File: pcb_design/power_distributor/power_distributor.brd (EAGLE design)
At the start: 34.3 x 34.3 mm, 12 parts

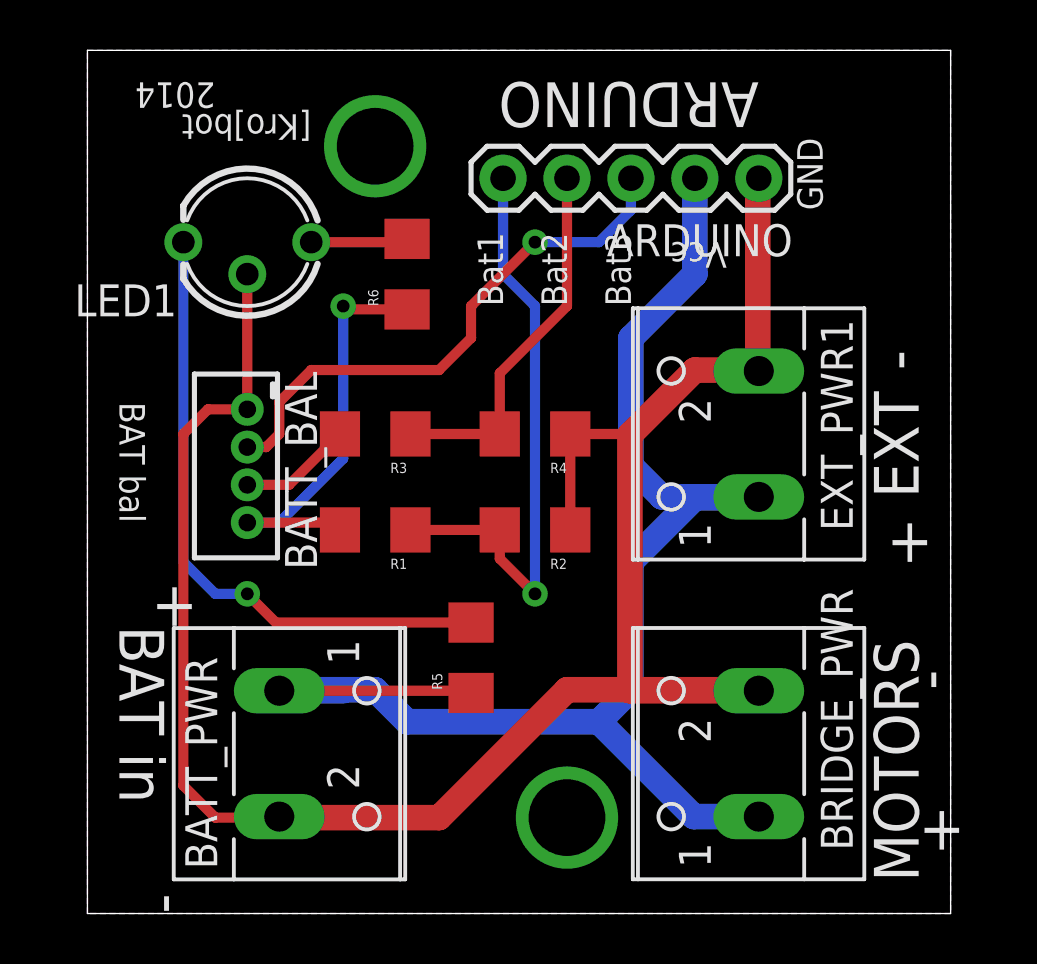
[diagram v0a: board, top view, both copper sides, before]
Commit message: [PCB/power_distributor] Correcting wrong JST footprint
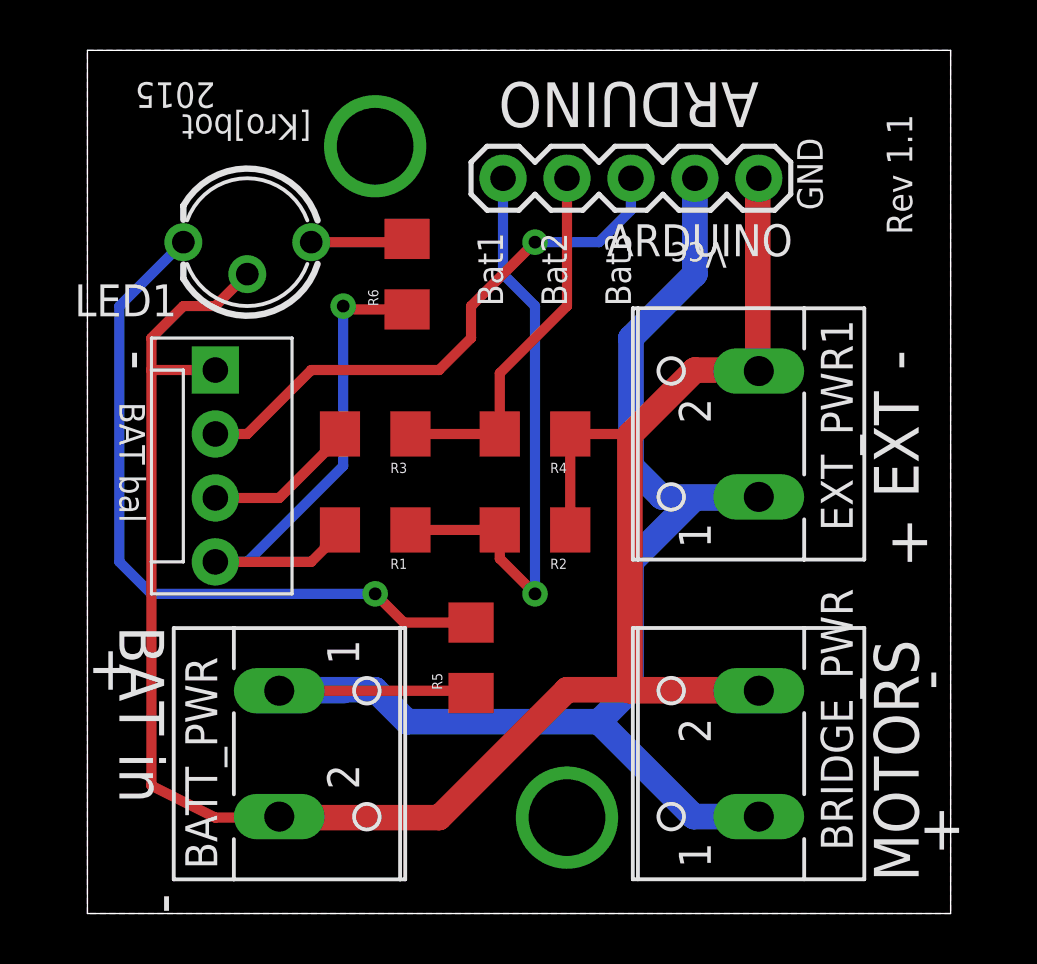
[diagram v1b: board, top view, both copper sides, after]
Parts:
- BATT_BAL: value B4B-ZR -> (none); device con-jst:B4B-ZR -> SparkFun-Connectors:MOLEX-1X4
- moved BATT_BAL 4.02 mm to (5.08, 21.6)
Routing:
- net VCC: track 17.3 -> 21.7 mm
- net GND: track 83.2 -> 87.1 mm
- net N$1: track 25.1 -> 28.7 mm
- net N$2: track 4.52 -> 6.08 mm
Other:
- board text added: "2015"
- board text added: "Rev 1.1"
- board text removed: "2014"
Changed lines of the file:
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@@
 <?xml version="1.0" encoding="utf-8"?>
 <!DOCTYPE eagle SYSTEM "eagle.dtd">
-<eagle version="7.1.0">
+<eagle version="6.5.0">
 <drawing>
 <settings>
@@
 <layers>
 <layer number="1" name="Top" color="4" fill="1" visible="yes" active="yes"/>
+<layer number="2" name="Route2" color="1" fill="3" visible="no" active="no"/>
+<layer number="3" name="Route3" color="4" fill="3" visible="no" active="no"/>
+<layer number="4" name="Route4" color="1" fill="4" visible="no" active="no"/>
+<layer number="5" name="Route5" color="4" fill="4" visible="no" active="no"/>
+<layer number="6" name="Route6" color="1" fill="8" visible="no" active="no"/>
+<layer number="7" name="Route7" color="4" fill="8" visible="no" active="no"/>
+<layer number="8" name="Route8" color="1" fill="2" visible="no" active="no"/>
+<layer number="9" name="Route9" color="4" fill="2" visible="no" active="no"/>
+<layer number="10" name="Route10" color="1" fill="7" visible="no" active="no"/>
+<layer number="11" name="Route11" color="4" fill="7" visible="no" active="no"/>
+<layer number="12" name="Route12" color="1" fill="5" visible="no" active="no"/>
+<layer number="13" name="Route13" color="4" fill="5" visible="no" active="no"/>
+<layer number="14" name="Route14" color="1" fill="6" visible="no" active="no"/>
+<layer number="15" name="Route15" color="4" fill="6" visible="no" active="no"/>
 <layer number="16" name="Bottom" color="1" fill="1" visible="yes" active="yes"/>
 <layer number="17" name="Pads" color="2" fill="1" visible="yes" active="yes"/>
@@
 <text x="19.05" y="24.13" size="1.016" layer="21" font="vector" ratio="15" rot="R90">Bat2</text>
 <text x="8.89" y="31.75" size="1.016" layer="21" font="vector" ratio="15" rot="SR180">[Kro]bot</text>
-<text x="5.08" y="33.02" size="1.016" layer="21" font="vector" ratio="15" rot="SR180">2014</text>
-<text x="2.54" y="11.43" size="1.778" layer="21" font="vector" ratio="15">+</text>
+<text x="5.08" y="33.02" size="1.016" layer="21" font="vector" ratio="15" rot="SR180">2015</text>
+<text x="0" y="8.89" size="1.778" layer="21" font="vector" ratio="15">+</text>
 <text x="33.02" y="2.54" size="1.778" layer="21" font="vector" ratio="15">+</text>
 <text x="31.75" y="13.97" size="1.778" layer="21" font="vector" ratio="15">+</text>
@@
 <dimension x1="0" y1="34.29" x2="0" y2="0" x3="-5.08" y3="17.145" textsize="1.778" textratio="15" layer="150"/>
 <dimension x1="0" y1="0" x2="34.29" y2="0" x3="17.145" y3="-6.35" textsize="1.778" textratio="15" layer="150"/>
+<text x="31.75" y="31.75" size="1.016" layer="21" font="vector" ratio="15" rot="R270">Rev 1.1</text>
+<text x="2.54" y="21.59" size="1.778" layer="21" font="vector" ratio="15" rot="R90">-</text>
 </plain>
 <attributes>
@@
 <pass name="Default">
 <param name="RoutingGrid" value="50mil"/>
-<param name="AutoGrid" value="1"/>
-<param name="Efforts" value="0"/>
-<param name="TopRouterVariant" value="1"/>
 <param name="tpViaShape" value="round"/>
-<param name="PrefDir.1" value="a"/>
+<param name="PrefDir.1" value="|"/>
 <param name="PrefDir.2" value="0"/>
 <param name="PrefDir.3" value="0"/>
@@
 <param name="PrefDir.14" value="0"/>
 <param name="PrefDir.15" value="0"/>
-<param name="PrefDir.16" value="a"/>
+<param name="PrefDir.16" value="-"/>
 <param name="cfVia" value="8"/>
 <param name="cfNonPref" value="5"/>
@@
 <elements>
 <element name="ARDUINO" library="SparkFun-Connectors" package="1X05" value="" x="26.67" y="29.21" rot="R180"/>
-<element name="BATT_BAL" library="con-jst" package="B4B-ZR" value="B4B-ZR" x="6.35" y="17.78" rot="R270">
-<attribute name="OC_NEWARK" value="37K9960" x="6.35" y="17.78" size="1.778" layer="27" rot="R270" display="off"/>
-<attribute name="MPN" value="B4B-ZR(LF)(SN)" x="6.35" y="17.78" size="1.778" layer="27" rot="R270" display="off"/>
-<attribute name="MF" value="FARNELL" x="6.35" y="17.78" size="1.778" layer="27" rot="R270" display="off"/>
-<attribute name="OC_FARNELL" value="1830916" x="6.35" y="17.78" size="1.778" layer="27" rot="R270" display="off"/>
-</element>
 <element name="BATT_PWR" library="con-wago-500" package="W237-102" value="" x="8.89" y="6.35" rot="R270">
 <attribute name="OC_NEWARK" value="70K9898" x="8.89" y="6.35" size="1.778" layer="27" rot="R270" display="off"/>
@@
 <element name="R5" library="SparkFun-Passives" package="1206" value="1000" x="15.24" y="10.16" rot="R90"/>
 <element name="R6" library="SparkFun-Passives" package="1206" value="1000" x="12.7" y="25.4" rot="R90"/>
+<element name="BATT_BAL" library="SparkFun-Connectors" package="MOLEX-1X4" value="" x="5.08" y="21.59" rot="R270"/>
 </elements>
 <signals>
 <signal name="VCC">
-<contactref element="BATT_BAL" pad="4"/>
 <contactref element="R1" pad="2"/>
 <contactref element="R6" pad="1"/>
-<wire x1="6.35" y1="15.53" x2="9.74" y2="15.53" width="0.4064" layer="1"/>
 <wire x1="9.74" y1="15.53" x2="10.03" y2="15.24" width="0.4064" layer="1"/>
 <wire x1="12.7" y1="24" x2="10.29" y2="24" width="0.4064" layer="1"/>
 <wire x1="10.29" y1="24" x2="10.16" y2="24.13" width="0.4064" layer="1"/>
 <via x="10.16" y="24.13" extent="1-16" drill="0.508"/>
-<wire x1="10.16" y1="24.13" x2="10.16" y2="18.07" width="0.4064" layer="16"/>
-<wire x1="10.16" y1="18.07" x2="7.62" y2="15.53" width="0.4064" layer="16"/>
-<wire x1="7.62" y1="15.53" x2="6.35" y2="15.53" width="0.4064" layer="16"/>
+<wire x1="10.16" y1="24.13" x2="10.16" y2="17.78" width="0.4064" layer="16"/>
+<contactref element="BATT_BAL" pad="4"/>
+<wire x1="9.74" y1="15.53" x2="9.74" y2="14.82" width="0.4064" layer="1"/>
+<wire x1="9.74" y1="14.82" x2="8.89" y2="13.97" width="0.4064" layer="1"/>
+<wire x1="8.89" y1="13.97" x2="5.08" y2="13.97" width="0.4064" layer="1"/>
+<wire x1="10.16" y1="17.78" x2="6.35" y2="13.97" width="0.4064" layer="16"/>
+<wire x1="6.35" y1="13.97" x2="5.08" y2="13.97" width="0.4064" layer="16"/>
 </signal>
 <signal name="BATT_1">
@@
 </signal>
 <signal name="N$2">
+<contactref element="R3" pad="2"/>
 <contactref element="BATT_BAL" pad="3"/>
-<contactref element="R3" pad="2"/>
-<wire x1="6.35" y1="17.03" x2="8.01" y2="17.03" width="0.4064" layer="1"/>
-<wire x1="8.01" y1="17.03" x2="10.03" y2="19.05" width="0.4064" layer="1"/>
+<wire x1="10.03" y1="19.05" x2="10.03" y2="18.92" width="0.4064" layer="1"/>
+<wire x1="10.03" y1="18.92" x2="7.62" y2="16.51" width="0.4064" layer="1"/>
+<wire x1="7.62" y1="16.51" x2="5.08" y2="16.51" width="0.4064" layer="1"/>
 </signal>
 <signal name="BATT_2">
@@
 <contactref element="R2" pad="1"/>
 <contactref element="R4" pad="1"/>
-<contactref element="BATT_BAL" pad="1"/>
 <contactref element="BATT_PWR" pad="2"/>
 <contactref element="LED1" pad="CC"/>
@@
 <contactref element="EXT_PWR1" pad="2"/>
 <wire x1="19.18" y1="15.24" x2="19.18" y2="19.05" width="0.4064" layer="1"/>
-<wire x1="6.35" y1="20.03" x2="6.35" y2="25.4" width="0.4064" layer="1"/>
-<wire x1="6.35" y1="20.03" x2="4.79" y2="20.03" width="0.4064" layer="1"/>
-<wire x1="4.79" y1="20.03" x2="3.81" y2="19.05" width="0.4064" layer="1"/>
-<wire x1="3.81" y1="19.05" x2="3.81" y2="5.08" width="0.4064" layer="1"/>
-<wire x1="3.81" y1="5.08" x2="5.08" y2="3.81" width="0.4064" layer="1"/>
+<wire x1="2.54" y1="22.86" x2="2.54" y2="21.59" width="0.4064" layer="1"/>
+<wire x1="2.54" y1="21.59" x2="2.54" y2="5.08" width="0.4064" layer="1"/>
+<wire x1="2.54" y1="5.08" x2="5.08" y2="3.81" width="0.4064" layer="1"/>
 <wire x1="5.08" y1="3.81" x2="7.58" y2="3.81" width="0.4064" layer="1"/>
 <wire x1="7.58" y1="3.81" x2="7.62" y2="3.85" width="0.4064" layer="1"/>
@@
 <vertex x="34.29" y="0"/>
 </polygon>
+<contactref element="BATT_BAL" pad="1"/>
+<wire x1="2.54" y1="22.86" x2="3.81" y2="24.13" width="0.4064" layer="1"/>
+<wire x1="3.81" y1="24.13" x2="5.08" y2="24.13" width="0.4064" layer="1"/>
+<wire x1="5.08" y1="24.13" x2="6.35" y2="25.4" width="0.4064" layer="1"/>
+<wire x1="5.08" y1="21.59" x2="2.54" y2="21.59" width="0.4064" layer="1"/>
 </signal>
 <signal name="BATT_3">
-<contactref element="BATT_BAL" pad="2"/>
 <contactref element="ARDUINO" pad="3"/>
-<wire x1="6.35" y1="18.53" x2="7.1" y2="18.53" width="0.4064" layer="1"/>
-<wire x1="7.1" y1="18.53" x2="7.62" y2="19.05" width="0.4064" layer="1"/>
-<wire x1="7.62" y1="19.05" x2="7.62" y2="20.32" width="0.4064" layer="1"/>
-<wire x1="7.62" y1="20.32" x2="8.89" y2="21.59" width="0.4064" layer="1"/>
 <wire x1="8.89" y1="21.59" x2="13.97" y2="21.59" width="0.4064" layer="1"/>
 <wire x1="13.97" y1="21.59" x2="15.24" y2="22.86" width="0.4064" layer="1"/>
@@
 <wire x1="20.32" y1="26.67" x2="21.59" y2="27.94" width="0.4064" layer="16"/>
 <wire x1="21.59" y1="27.94" x2="21.59" y2="29.21" width="0.4064" layer="16"/>
+<contactref element="BATT_BAL" pad="2"/>
+<wire x1="8.89" y1="21.59" x2="6.35" y2="19.05" width="0.4064" layer="1"/>
+<wire x1="6.35" y1="19.05" x2="5.08" y2="19.05" width="0.4064" layer="1"/>
 </signal>
 <signal name="VDD">
@@
 <contactref element="R5" pad="2"/>
 <contactref element="LED1" pad="AO"/>
-<wire x1="15.24" y1="11.56" x2="7.49" y2="11.56" width="0.4064" layer="1"/>
-<wire x1="7.49" y1="11.56" x2="6.35" y2="12.7" width="0.4064" layer="1"/>
-<via x="6.35" y="12.7" extent="1-16" drill="0.508"/>
-<wire x1="6.35" y1="12.7" x2="5.08" y2="12.7" width="0.4064" layer="16"/>
-<wire x1="5.08" y1="12.7" x2="3.81" y2="13.97" width="0.4064" layer="16"/>
-<wire x1="3.81" y1="13.97" x2="3.81" y2="26.67" width="0.4064" layer="16"/>
+<wire x1="15.24" y1="11.56" x2="12.57" y2="11.56" width="0.4064" layer="1"/>
+<wire x1="12.57" y1="11.56" x2="11.43" y2="12.7" width="0.4064" layer="1"/>
+<via x="11.43" y="12.7" extent="1-16" drill="0.508"/>
+<wire x1="11.43" y1="12.7" x2="2.54" y2="12.7" width="0.4064" layer="16"/>
+<wire x1="2.54" y1="12.7" x2="1.27" y2="13.97" width="0.4064" layer="16"/>
+<wire x1="1.27" y1="13.97" x2="1.27" y2="24.13" width="0.4064" layer="16"/>
+<wire x1="1.27" y1="24.13" x2="3.81" y2="26.67" width="0.4064" layer="16"/>
 </signal>
 <signal name="N$3">
